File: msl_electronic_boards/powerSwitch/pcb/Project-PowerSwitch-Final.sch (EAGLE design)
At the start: 130 parts, among them IC10 BTS6133, IC11 BTS6133, IC12 BTS6133, IC15 BTS6133, IC3 LM2574M-5.0, IC4 BTS555E3146, IC7 MAX202, Q1 16Mhz, T1 BC847, T2 BC849, T5 BC849, T6 BC849, T7 BC849

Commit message: PCB PowerSwitch
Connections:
- net SW_12V: now also U$2.PD7
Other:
- moved on the sheet: JP6, JP7
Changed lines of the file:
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@@
 <attribute name="VALUE" x="0" y="160.02" size="1.778" layer="96"/>
 </instance>
-<instance part="JP6" gate="1" x="121.92" y="109.22" rot="MR270"/>
-<instance part="JP7" gate="1" x="121.92" y="99.06" rot="MR270"/>
+<instance part="JP6" gate="1" x="127" y="109.22" rot="MR270"/>
+<instance part="JP7" gate="1" x="127" y="99.06" rot="MR270"/>
 <instance part="SV4" gate="G$1" x="233.68" y="114.3"/>
 <instance part="P+7" gate="1" x="220.98" y="121.92" smashed="yes">
@@
 <net name="TXD" class="0">
 <segment>
-<wire x1="124.46" y1="96.52" x2="127" y2="96.52" width="0.1524" layer="91"/>
-<label x="127" y="96.52" size="1.27" layer="95" xref="yes"/>
+<wire x1="129.54" y1="96.52" x2="132.08" y2="96.52" width="0.1524" layer="91"/>
+<label x="132.08" y="96.52" size="1.27" layer="95" xref="yes"/>
 <pinref part="JP7" gate="1" pin="3"/>
 </segment>
@@
 <net name="RXD" class="0">
 <segment>
-<wire x1="124.46" y1="106.68" x2="127" y2="106.68" width="0.1524" layer="91"/>
-<label x="127" y="106.68" size="1.27" layer="95" xref="yes"/>
+<wire x1="129.54" y1="106.68" x2="132.08" y2="106.68" width="0.1524" layer="91"/>
+<label x="132.08" y="106.68" size="1.27" layer="95" xref="yes"/>
 <pinref part="JP6" gate="1" pin="3"/>
 </segment>
@@
 <net name="SCK" class="0">
 <segment>
-<label x="127" y="111.76" size="1.27" layer="95" xref="yes"/>
-<wire x1="124.46" y1="111.76" x2="127" y2="111.76" width="0.1524" layer="91"/>
+<label x="132.08" y="111.76" size="1.27" layer="95" xref="yes"/>
+<wire x1="129.54" y1="111.76" x2="132.08" y2="111.76" width="0.1524" layer="91"/>
 <pinref part="JP6" gate="1" pin="1"/>
 </segment>
@@
 <net name="MOSI" class="0">
 <segment>
-<label x="127" y="101.6" size="1.27" layer="95" xref="yes"/>
-<wire x1="124.46" y1="101.6" x2="127" y2="101.6" width="0.1524" layer="91"/>
+<label x="132.08" y="101.6" size="1.27" layer="95" xref="yes"/>
+<wire x1="129.54" y1="101.6" x2="132.08" y2="101.6" width="0.1524" layer="91"/>
 <pinref part="JP7" gate="1" pin="1"/>
 </segment>
@@
 <label x="223.52" y="134.62" size="1.27" layer="95" rot="R180" xref="yes"/>
 <pinref part="SV2" gate="G$1" pin="4"/>
+</segment>
+<segment>
+<wire x1="96.52" y1="111.76" x2="106.68" y2="111.76" width="0.1524" layer="91"/>
+<label x="106.68" y="111.76" size="1.27" layer="95" xref="yes"/>
+<pinref part="U$2" gate="G$1" pin="PD7"/>
 </segment>
 </net>
@@
 <pinref part="JP6" gate="1" pin="2"/>
 <pinref part="U$2" gate="G$1" pin="(RXD)PD4"/>
-<wire x1="124.46" y1="109.22" x2="116.84" y2="109.22" width="0.1524" layer="91"/>
-<wire x1="116.84" y1="109.22" x2="116.84" y2="104.14" width="0.1524" layer="91"/>
-<wire x1="116.84" y1="104.14" x2="96.52" y2="104.14" width="0.1524" layer="91"/>
+<wire x1="129.54" y1="109.22" x2="121.92" y2="109.22" width="0.1524" layer="91"/>
+<wire x1="121.92" y1="109.22" x2="121.92" y2="104.14" width="0.1524" layer="91"/>
+<wire x1="121.92" y1="104.14" x2="96.52" y2="104.14" width="0.1524" layer="91"/>
 </segment>
 </net>
@@
 <segment>
 <pinref part="JP7" gate="1" pin="2"/>
-<wire x1="124.46" y1="99.06" x2="116.84" y2="99.06" width="0.1524" layer="91"/>
-<wire x1="116.84" y1="99.06" x2="116.84" y2="101.6" width="0.1524" layer="91"/>
+<wire x1="129.54" y1="99.06" x2="121.92" y2="99.06" width="0.1524" layer="91"/>
+<wire x1="121.92" y1="99.06" x2="121.92" y2="101.6" width="0.1524" layer="91"/>
 <pinref part="U$2" gate="G$1" pin="(MOSI_A/TXD)PD3"/>
-<wire x1="116.84" y1="101.6" x2="96.52" y2="101.6" width="0.1524" layer="91"/>
-</segment>
-</net>
+<wire x1="121.92" y1="101.6" x2="96.52" y2="101.6" width="0.1524" layer="91"/>
+</segment>
+</net>

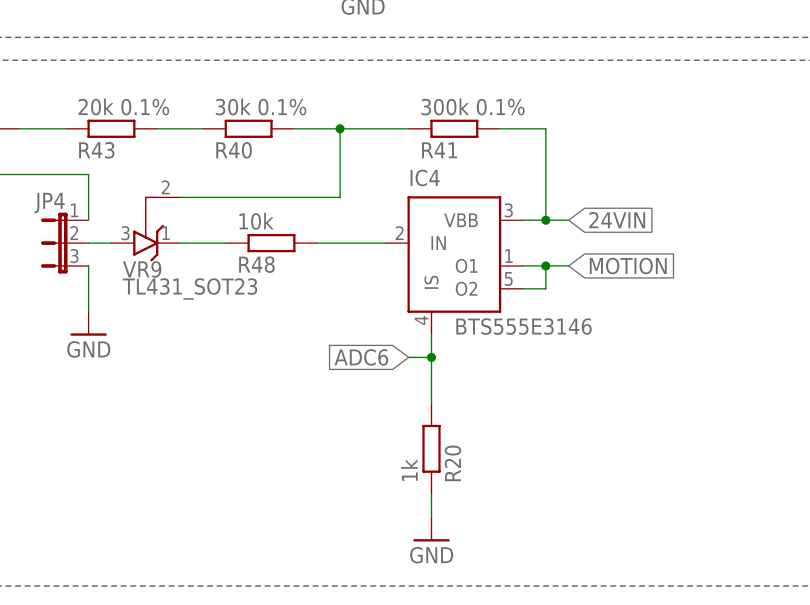
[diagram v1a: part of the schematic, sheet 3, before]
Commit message: PowerSwitch
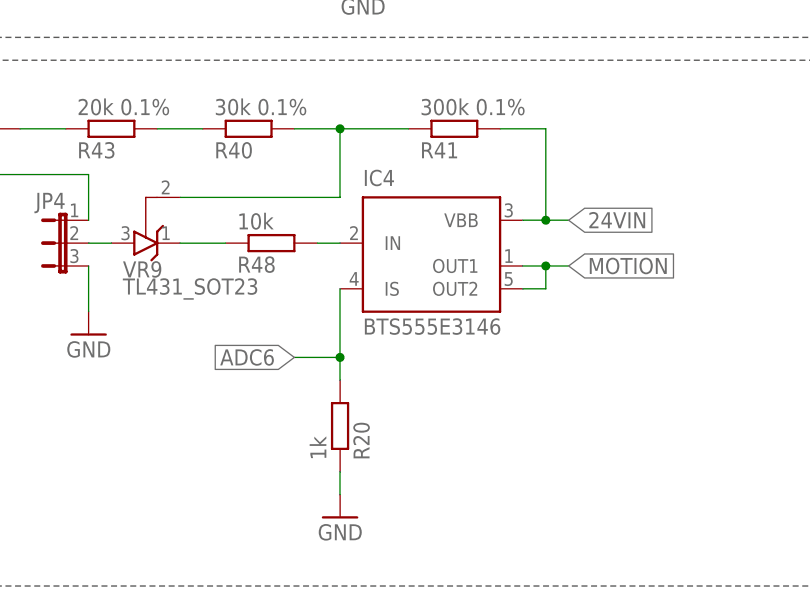
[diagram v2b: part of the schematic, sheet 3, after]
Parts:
- IC4: device infineon:BTS555E3146 -> micro-siemens:BTS555E3146
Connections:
- net MOTION: now also IC4.OUT1, IC4.OUT2; no longer IC4.O1, IC4.O2
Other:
- moved on the sheet: IC4, R20
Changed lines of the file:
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@@
 <part name="RS232" library="con-ml" deviceset="ML6" device=""/>
 <part name="FRAME3" library="frames" deviceset="DINA4_L" device=""/>
-<part name="IC4" library="infineon" deviceset="BTS555" device="E3146"/>
+<part name="IC4" library="micro-siemens" deviceset="BTS555" device="E3146"/>
 <part name="IC10" library="BTS443P" deviceset="BTS6133" device=""/>
 <part name="IC11" library="BTS443P" deviceset="BTS6133" device=""/>
@@
 <instance part="FRAME3" gate="G$1" x="0" y="0"/>
 <instance part="FRAME3" gate="G$2" x="162.56" y="0"/>
-<instance part="IC4" gate="G$1" x="76.2" y="38.1"/>
+<instance part="IC4" gate="G$1" x="73.66" y="40.64"/>
 <instance part="IC10" gate="G$1" x="228.6" y="91.44"/>
 <instance part="IC11" gate="G$1" x="78.74" y="157.48"/>
@@
 <instance part="R14" gate="G$1" x="66.04" y="78.74" rot="MR90"/>
 <instance part="R19" gate="G$1" x="66.04" y="139.7" rot="MR90"/>
-<instance part="R20" gate="G$1" x="73.66" y="17.78" rot="MR90"/>
+<instance part="R20" gate="G$1" x="63.5" y="20.32" rot="MR90"/>
 <instance part="R21" gate="G$1" x="215.9" y="147.32" rot="MR90"/>
 <instance part="GND1" gate="1" x="215.9" y="60.96" rot="MR0"/>
@@
 <instance part="GND4" gate="1" x="66.04" y="68.58" rot="MR0"/>
 <instance part="GND5" gate="1" x="66.04" y="129.54" rot="MR0"/>
-<instance part="GND31" gate="1" x="73.66" y="7.62" rot="MR0"/>
+<instance part="GND31" gate="1" x="63.5" y="10.16" rot="MR0"/>
 <instance part="GND32" gate="1" x="154.94" y="119.38" rot="MR0"/>
 <instance part="GND35" gate="1" x="38.1" y="144.78" rot="MR0"/>
@@
 </segment>
 <segment>
-<wire x1="73.66" y1="12.7" x2="73.66" y2="10.16" width="0.1524" layer="91"/>
+<wire x1="63.5" y1="15.24" x2="63.5" y2="12.7" width="0.1524" layer="91"/>
 <pinref part="R20" gate="G$1" pin="1"/>
 <pinref part="GND31" gate="1" pin="GND"/>
@@
 <net name="MOTION" class="0">
 <segment>
-<wire x1="83.82" y1="35.56" x2="86.36" y2="35.56" width="0.1524" layer="91"/>
 <wire x1="86.36" y1="35.56" x2="86.36" y2="38.1" width="0.1524" layer="91"/>
 <wire x1="88.9" y1="38.1" x2="86.36" y2="38.1" width="0.1524" layer="91"/>
-<wire x1="86.36" y1="38.1" x2="83.82" y2="38.1" width="0.1524" layer="91"/>
+<label x="88.9" y="38.1" size="1.778" layer="95" xref="yes"/>
+<pinref part="IC4" gate="G$1" pin="OUT1"/>
+<wire x1="83.82" y1="38.1" x2="86.36" y2="38.1" width="0.1524" layer="91"/>
 <junction x="86.36" y="38.1"/>
-<label x="88.9" y="38.1" size="1.778" layer="95" xref="yes"/>
-<pinref part="IC4" gate="G$1" pin="O2"/>
-<pinref part="IC4" gate="G$1" pin="O1"/>
+<pinref part="IC4" gate="G$1" pin="OUT2"/>
+<wire x1="83.82" y1="35.56" x2="86.36" y2="35.56" width="0.1524" layer="91"/>
 </segment>
 </net>
@@
 <net name="N$46" class="0">
 <segment>
-<wire x1="60.96" y1="40.64" x2="68.58" y2="40.64" width="0.1524" layer="91"/>
+<wire x1="60.96" y1="40.64" x2="63.5" y2="40.64" width="0.1524" layer="91"/>
 <pinref part="IC4" gate="G$1" pin="IN"/>
 <pinref part="R48" gate="G$1" pin="2"/>
@@
 <net name="ADC6" class="0">
 <segment>
-<wire x1="73.66" y1="30.48" x2="73.66" y2="27.94" width="0.1524" layer="91"/>
-<wire x1="73.66" y1="27.94" x2="73.66" y2="22.86" width="0.1524" layer="91"/>
-<wire x1="73.66" y1="27.94" x2="71.12" y2="27.94" width="0.1524" layer="91"/>
-<junction x="73.66" y="27.94"/>
-<label x="71.12" y="27.94" size="1.778" layer="95" rot="R180" xref="yes"/>
+<wire x1="63.5" y1="35.56" x2="63.5" y2="27.94" width="0.1524" layer="91"/>
+<wire x1="63.5" y1="27.94" x2="63.5" y2="25.4" width="0.1524" layer="91"/>
+<wire x1="63.5" y1="27.94" x2="58.42" y2="27.94" width="0.1524" layer="91"/>
+<junction x="63.5" y="27.94"/>
+<label x="58.42" y="27.94" size="1.778" layer="95" rot="R180" xref="yes"/>
 <pinref part="IC4" gate="G$1" pin="IS"/>
 <pinref part="R20" gate="G$1" pin="2"/>
